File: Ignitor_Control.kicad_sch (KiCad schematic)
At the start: 17 parts, among them J14 Ignitor Screw Terminal, K3 G5Q-1, K4 G5Q-1, Q4 BSS138, Q5 BSS138, U12 INA187A1

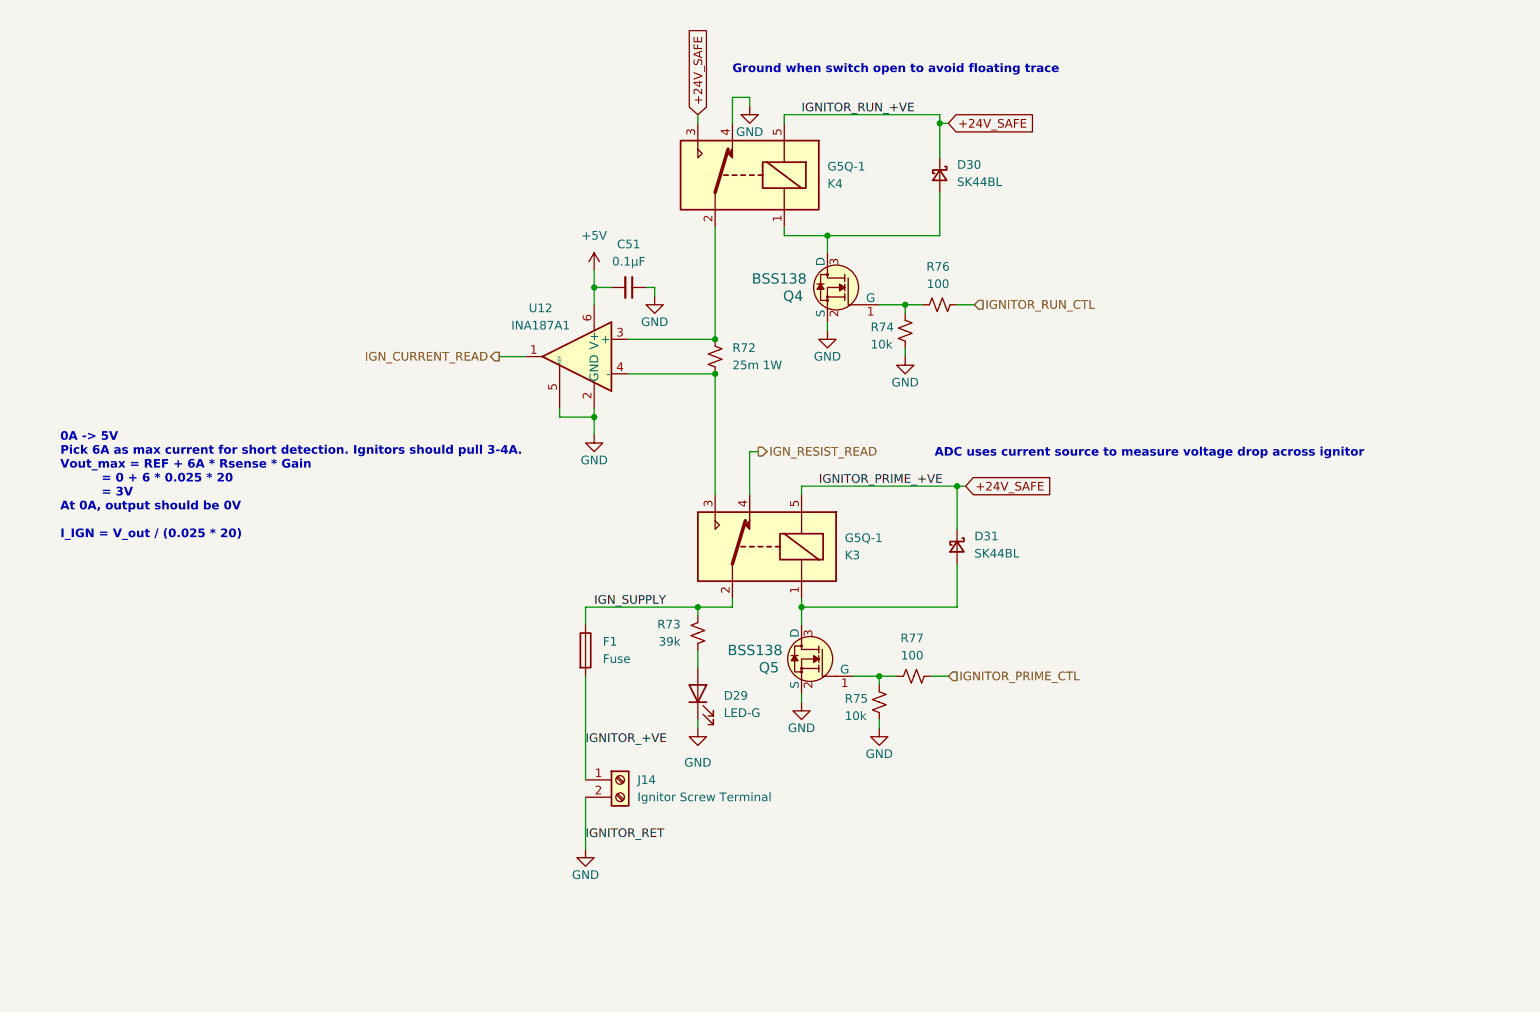
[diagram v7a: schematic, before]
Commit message: add rc filters to pressure transducer power in to filter 500khz signal on 24v rail
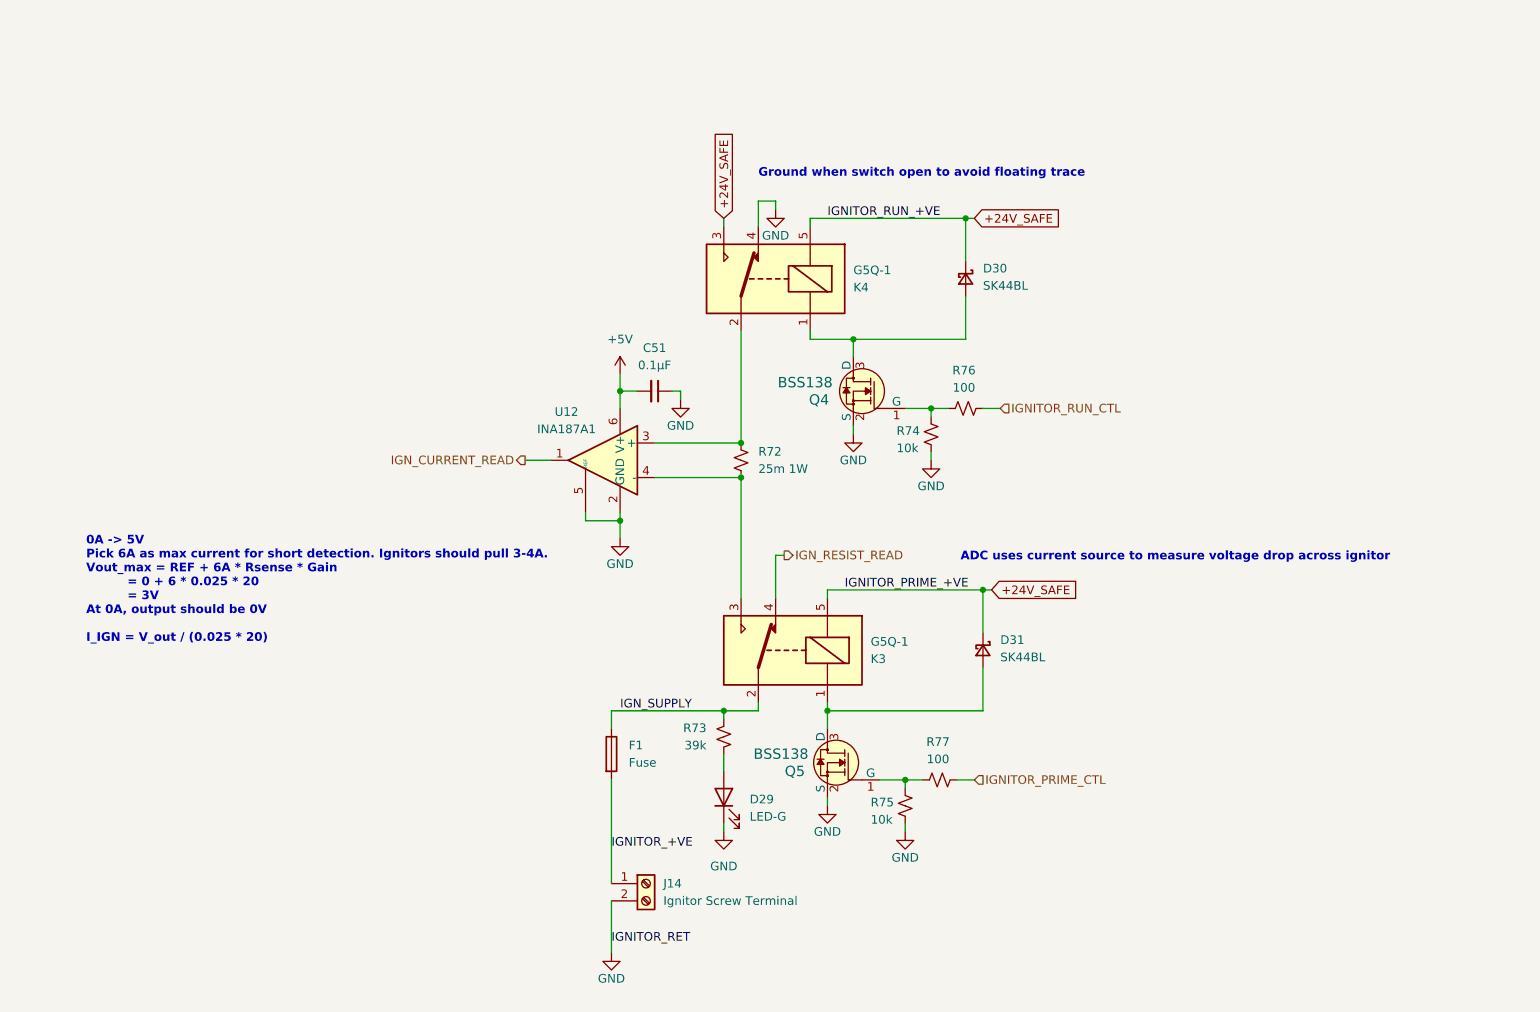
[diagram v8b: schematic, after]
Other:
- moved on the sheet: C51, D29, D30, D31, F1, J14, K3, K4, Q4, Q5, R72, R73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
